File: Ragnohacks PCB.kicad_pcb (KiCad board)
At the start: 2 copper layers, 85.6 x 54 mm, 35 parts, among them J1 Conn_01x02, J2 Conn_01x18, J3 Conn_01x18, J4 USB_A, SW1 SW_Push, U1 RP2040, U2 W25Q128JVS, U3 LD1117S33TR_SOT223, U4 USBLC6-2P6, Y1 12MHz

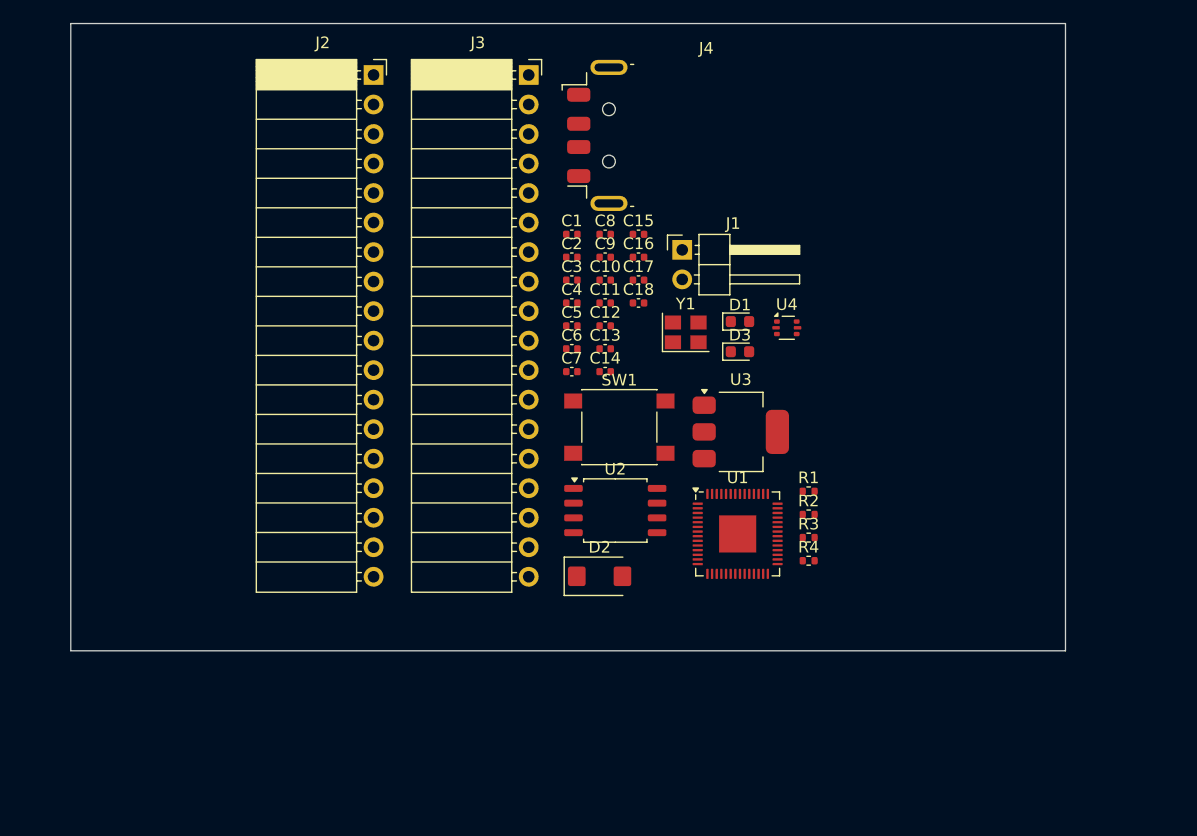
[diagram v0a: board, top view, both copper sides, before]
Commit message: Finish schematic and part choosing, get initial quote
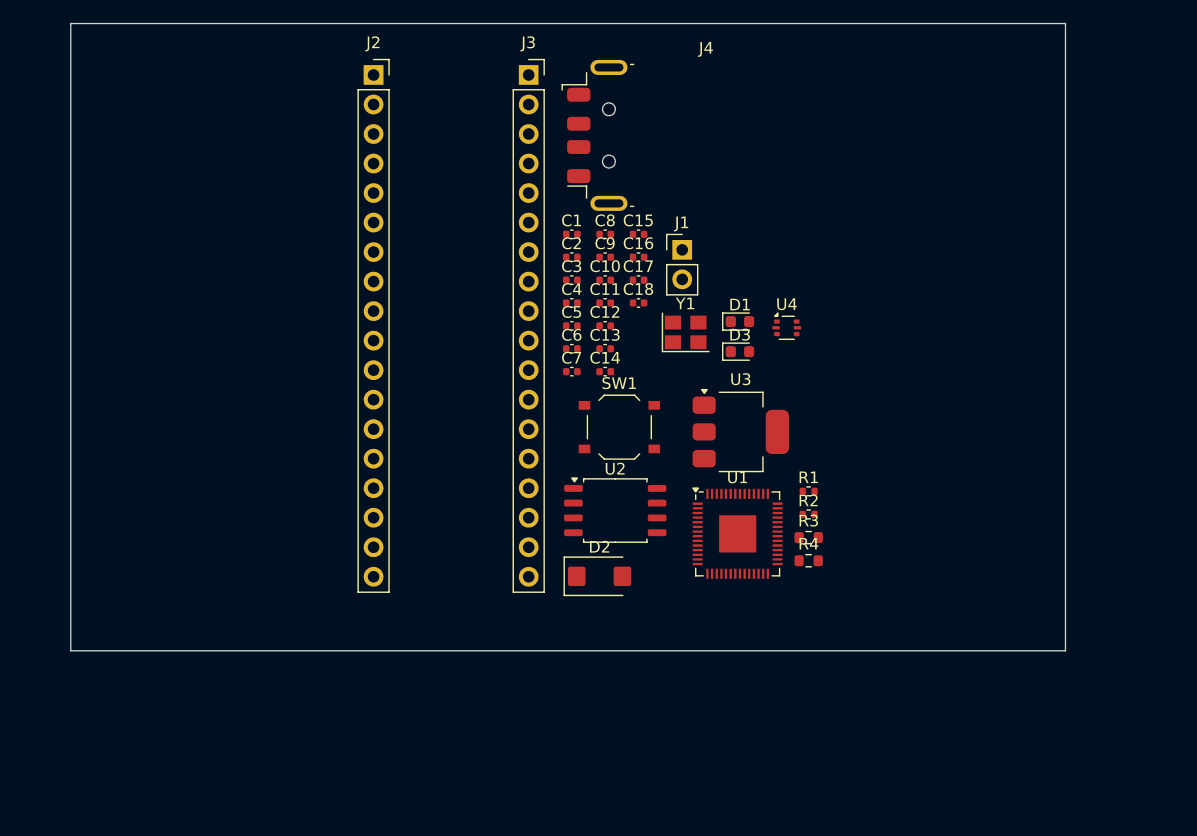
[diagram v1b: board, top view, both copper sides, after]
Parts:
- J1: footprint Connector_PinHeader_2.54mm:PinHeader_1x02_P2.54mm_Horizontal -> Connector_PinHeader_2.54mm:PinHeader_1x02_P2.54mm_Vertical
- J2, J3: footprint Connector_PinSocket_2.54mm:PinSocket_1x18_P2.54mm_Horizontal -> Connector_PinSocket_2.54mm:PinSocket_1x18_P2.54mm_Vertical
- R3, R4: value 460R -> 360R; footprint Resistor_SMD:R_0402_1005Metric -> Resistor_SMD:R_0603_1608Metric
- SW1: footprint Button_Switch_SMD:SW_Push_1P1T_NO_6x6mm_H9.5mm -> Button_Switch_SMD:SW_Push_1P1T_XKB_TS-1187A

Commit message: Start layout, add PCBWay parts
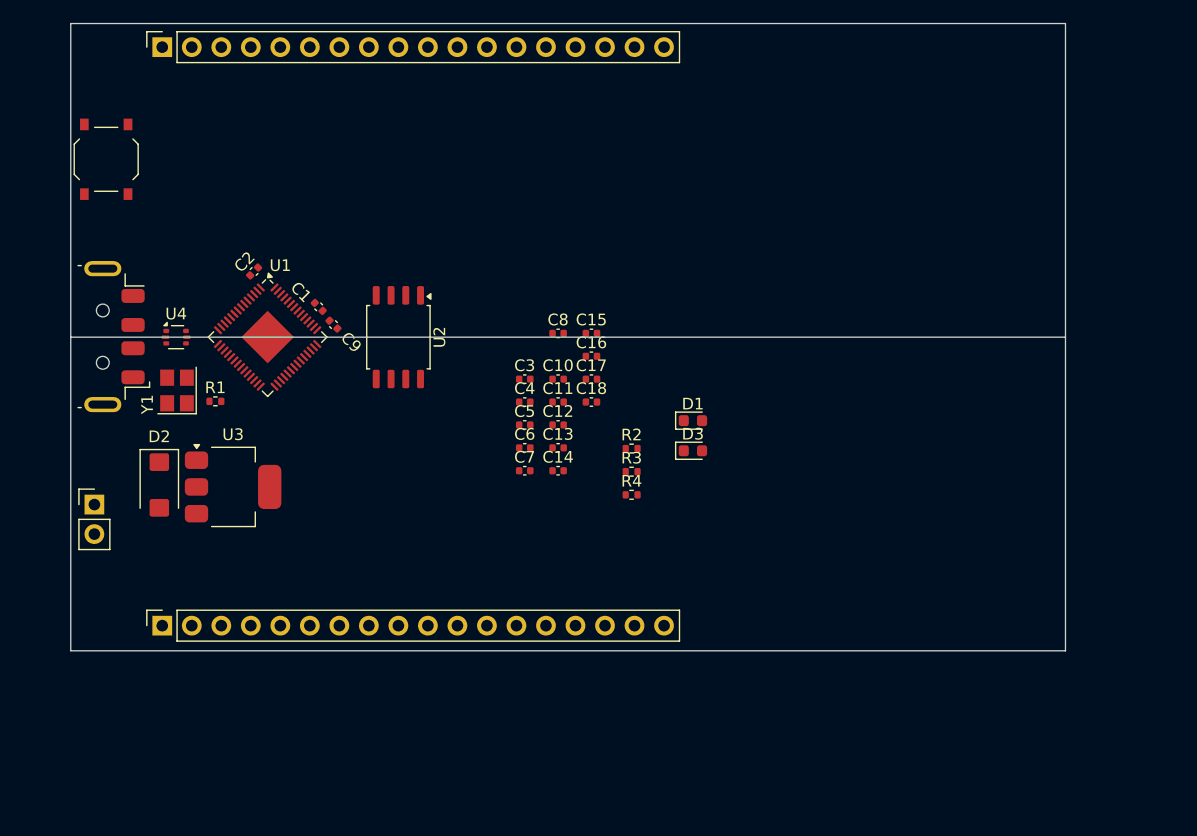
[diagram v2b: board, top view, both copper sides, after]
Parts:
- C13, C14: value 24pF -> 18pF
- R3, R4: footprint Resistor_SMD:R_0603_1608Metric -> Resistor_SMD:R_0402_1005Metric
- moved J4 62.7 mm to (88.6, 91.0), turned to 180 degrees
- moved J1 55.1 mm to (96.3, 105.4)
- moved U4 52.6 mm to (103.3, 91.0)
- moved R1 51.6 mm to (106.7, 96.5)
- moved J2 50.8 mm to (102.1, 115.8), turned to 90 degrees
- moved SW1 49.8 mm to (97.3, 75.7), turned to 90 degrees
- moved Y1 44.1 mm to (103.4, 95.6), turned to 90 degrees
- moved U3 43.9 mm to (108.2, 103.9)
- moved U1 43.8 mm to (111.2, 91.0), turned to -45 degrees
- moved D2 38.7 mm to (101.9, 103.7), turned to -90 degrees
- moved J3 31.6 mm to (102.1, 66.0), turned to 90 degrees
- moved C2 27.4 mm to (110.0, 85.3), turned to 45 degrees
- moved C9 24.1 mm to (116.8, 89.9), turned to -45 degrees
- moved U2 23.9 mm to (122.4, 91.0), turned to -90 degrees
- moved C1 22.7 mm to (115.6, 88.4), turned to -45 degrees
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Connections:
- U1 pad 11: D8 -> D17
- U1 pad 12: D9 -> D16
- U1 pad 13: D10 -> D15
- U1 pad 14: D11 -> D14
- U1 pad 15: D12 -> D13
- U1 pad 16: D13 -> D12
- U1 pad 17: D14 -> D11
- U1 pad 18: D15 -> D10
- U1 pad 2: D0 -> LED_25
- U1 pad 27: D16 -> D9
- U1 pad 28: D17 -> D8
- U1 pad 29: D18 -> D7
- U1 pad 3: D1 -> D24
- U1 pad 30: D19 -> D6
- U1 pad 31: D20 -> D5
- U1 pad 32: D21 -> D4
- U1 pad 34: D22 -> D3
- U1 pad 35: D23 -> D2
- U1 pad 36: D24 -> D1
- U1 pad 37: LED_25 -> D0
- U1 pad 38: A0 -> A3
- U1 pad 39: A1 -> A2
- U1 pad 4: D2 -> D23
- U1 pad 40: A2 -> A1
- U1 pad 41: A3 -> A0
- U1 pad 5: D3 -> D22
- U1 pad 6: D4 -> D21
- U1 pad 7: D5 -> D20
- U1 pad 8: D6 -> D19
- U1 pad 9: D7 -> D18
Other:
- outline, holes or cut-outs redrawn

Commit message: Start tracing
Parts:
- moved C17 44.2 mm to (107.4, 125.4), turned to 180 degrees
- moved R2 34.6 mm to (108.6, 93.9), turned to -90 degrees
- moved C18 33.0 mm to (117.0, 121.1), turned to -90 degrees
- moved C16 32.5 mm to (106.5, 93.4)
- moved C2 26.8 mm to (130.4, 102.7), turned to -45 degrees
- moved C1 24.9 mm to (128.3, 109.8)
- moved C8 23.0 mm to (123.0, 109.6), turned to -135 degrees
- moved J1 22.9 mm to (92.1, 128.0)
- moved C9 22.7 mm to (126.3, 110.6), turned to -135 degrees
- moved U2 19.8 mm to (135.5, 105.9)
- moved C13 19.3 mm to (117.4, 96.1), turned to -90 degrees
- moved C15 19.3 mm to (139.1, 109.9), turned to 90 degrees
- moved C10 19.0 mm to (127.1, 111.3), turned to -135 degrees
- moved U1 18.7 mm to (124.7, 103.9), turned to -135 degrees
- moved C14 18.3 mm to (120.1, 93.7)
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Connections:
- U1 pad 14: D14 -> D0
- U1 pad 15: D13 -> D1
- U1 pad 16: D12 -> D2
- U1 pad 17: D11 -> D3
- U1 pad 18: D10 -> D4
- U1 pad 27: D9 -> D5
- U1 pad 28: D8 -> D6
- U1 pad 30: D6 -> D8
- U1 pad 31: D5 -> D9
- U1 pad 32: D4 -> D10
- U1 pad 34: D3 -> D11
- U1 pad 35: D2 -> D12
- U1 pad 36: D1 -> D13
- U1 pad 37: D0 -> D14
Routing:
- net D0: track 0.00 -> 62.2 mm
- net D1: track 0.00 -> 59.4 mm
- net D2: track 0.00 -> 56.3 mm
- net D15: track 0.00 -> 28.4 mm
- net D16: track 0.00 -> 26.2 mm
- net D18: track 0.00 -> 26.1 mm
- net D19: track 0.00 -> 25.8 mm
- net D17: track 0.00 -> 25.7 mm
- net D24: track 0.00 -> 25.7 mm
- net D20: track 0.00 -> 25.6 mm
- net D21: track 0.00 -> 25.3 mm
- net D22: track 0.00 -> 25.1 mm
- net D23: track 0.00 -> 24.8 mm
- net +3V3: track 0.00 -> 20.5 mm
- net FLASH_CS: track 0.00 -> 12.9 mm
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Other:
- outline, holes or cut-outs redrawn
- board text added: "ON"

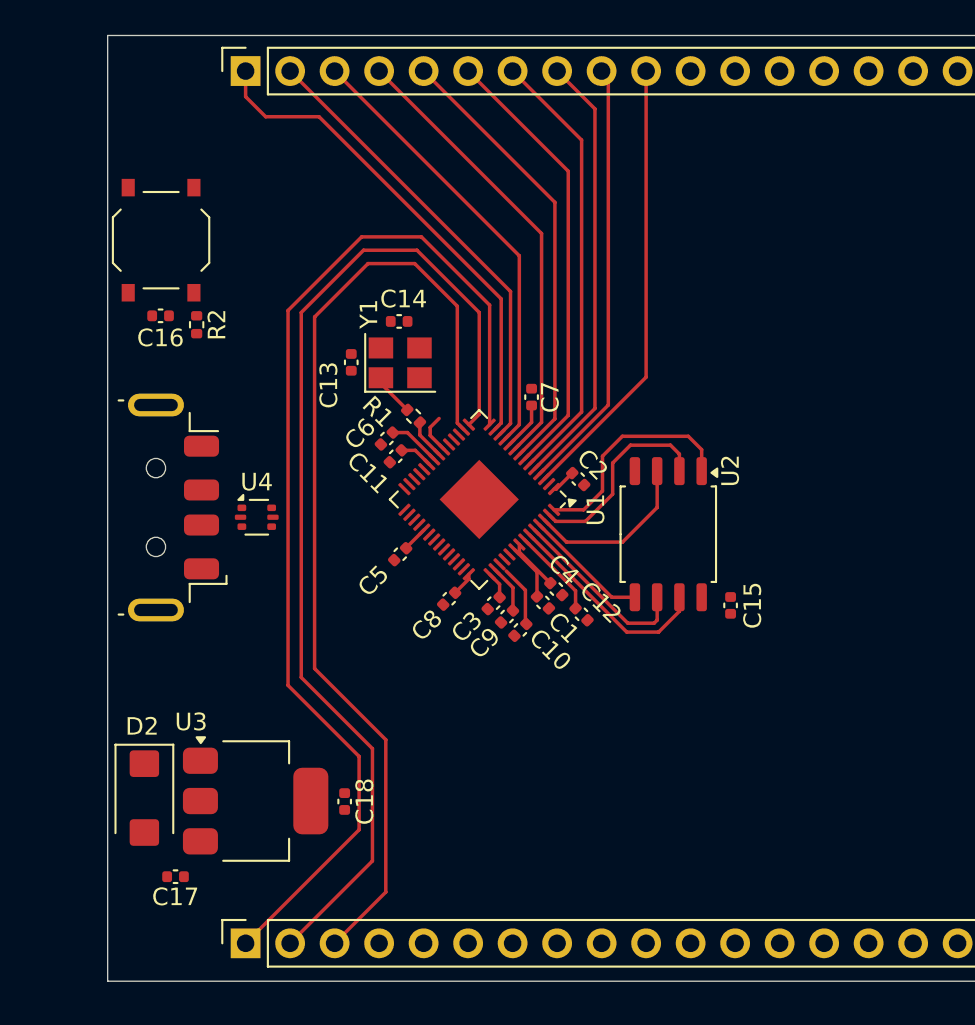
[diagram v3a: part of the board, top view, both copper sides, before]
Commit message: Finish tracing pins
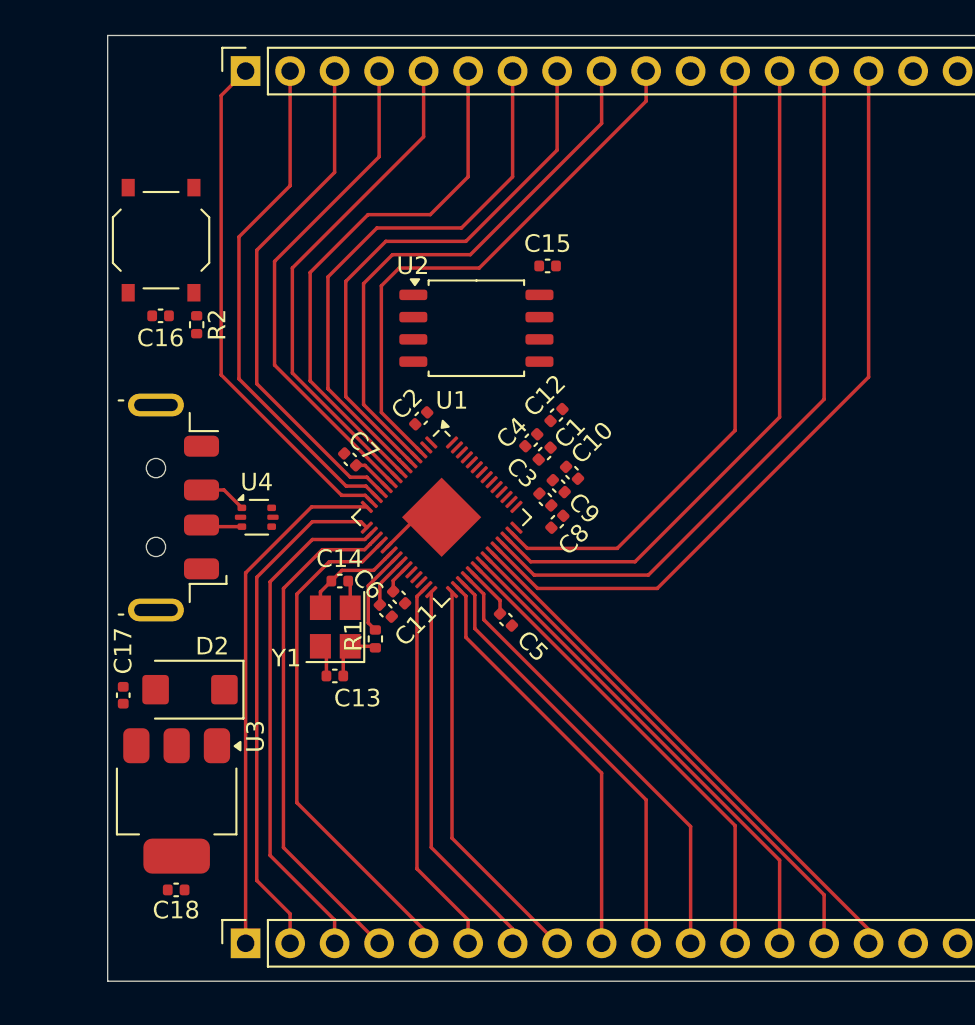
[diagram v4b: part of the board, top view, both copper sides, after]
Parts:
- moved C15 22.0 mm to (128.6, 90.6), turned to 180 degrees
- moved C13 17.9 mm to (116.5, 114.0), turned to 0 degrees
- moved U2 16.1 mm to (124.6, 94.1), turned to 0 degrees
- moved Y1 15.5 mm to (116.5, 111.2), turned to 90 degrees
- moved C14 15.2 mm to (116.8, 108.5), turned to 180 degrees
- moved R1 12.9 mm to (118.8, 111.8), turned to 90 degrees
- moved C12 11.5 mm to (129.1, 99.1), turned to 45 degrees
- moved C7 10.9 mm to (117.3, 101.6), turned to 135 degrees
- moved C18 10.9 mm to (107.4, 126.2), turned to 180 degrees
- moved C17 10.8 mm to (104.4, 115.1), turned to 90 degrees
- moved C6 9.83 mm to (119.4, 110.2), turned to -45 degrees
- moved C2 9.61 mm to (121.4, 99.3), turned to 45 degrees
- moved C10 9.44 mm to (130.0, 102.4), turned to -45 degrees
- moved C4 8.62 mm to (127.7, 100.5), turned to 45 degrees
- moved C1 8.50 mm to (128.4, 101.3), turned to 45 degrees
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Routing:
- net A3: track 0.00 -> 44.7 mm
- net A2: track 0.00 -> 42.1 mm
- net A1: track 0.00 -> 39.3 mm
- net A0: track 0.00 -> 36.4 mm
- net D0: track 62.2 -> 29.6 mm
- net D14: track 0.00 -> 31.2 mm
- net D13: track 0.00 -> 30.0 mm
- net D1: track 59.4 -> 29.4 mm
- net D3: track 0.00 -> 29.0 mm
- net D4: track 0.00 -> 29.0 mm
- net D12: track 0.00 -> 28.8 mm
- net D11: track 0.00 -> 27.6 mm
- net D2: track 56.3 -> 29.1 mm
- net D10: track 0.00 -> 26.2 mm
- net D9: track 0.00 -> 25.0 mm
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
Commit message: Finish tracing
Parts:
- moved J1 38.2 mm to (105.7, 92.2)
- moved R4 33.9 mm to (133.3, 90.7), turned to 90 degrees
- moved R3 30.6 mm to (135.9, 90.7), turned to 90 degrees
- moved D3 30.6 mm to (133.3, 93.2), turned to -90 degrees
- moved D1 26.7 mm to (135.9, 93.2), turned to -90 degrees
- moved C16 4.26 mm to (106.3, 89.2)
- moved R2 4.26 mm to (108.3, 89.7)
- moved SW1 4.25 mm to (106.4, 84.8)
- moved R1 2.07 mm to (118.5, 113.9), turned to 0 degrees
- moved C17 0.55 mm to (104.5, 115.6)
- moved C6 0.52 mm to (119.5, 110.7)
- moved C11 0.51 mm to (120.1, 110.0)
- moved C2 0.25 mm to (121.2, 99.3)
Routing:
- net +3V3: track 8.22 -> 180.3 mm, vias 0 -> 10
- net +5V: track 0.00 -> 122.2 mm, vias 0 -> 1
- net RESET: track 0.00 -> 121.5 mm, vias 0 -> 5
- net +1V1: track 1.69 -> 34.4 mm, vias 0 -> 2
- net USB_DP: track 0.00 -> 23.6 mm, vias 0 -> 2
- net Net-(J1-Pin_2): track 0.00 -> 23.2 mm, vias 0 -> 1
- net Net-(J1-Pin_1): track 0.00 -> 22.8 mm, vias 0 -> 1
- net USB_DN: track 0.00 -> 22.3 mm, vias 0 -> 2
- net LED_25: track 0.00 -> 17.8 mm, vias 0 -> 2
- net FLASH_CS: track 0.00 -> 12.7 mm
- net FLASH_SD3: track 0.00 -> 12.3 mm
- net FLASH_SD1: track 0.00 -> 11.9 mm
- net FLASH_CLK: track 0.00 -> 10.3 mm
- net GND: track 7.26 -> 17.4 mm, vias 0 -> 17
- net FLASH_SD2: track 0.00 -> 8.68 mm
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- added copper zone on B.Cu, net GND
- added copper zone on F.Cu, net GND

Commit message: The finishing touches
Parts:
- J4: footprint Connector_USB:USB_A_Molex_48037-2200_Horizontal -> Connector_USB:USB_A_Keystone_931_Horizontal
- moved J4 20.6 mm to (118.5, 104.3), turned to -90 degrees
- moved C16 2.84 mm to (108.0, 91.4), turned to 90 degrees
- moved R2 1.89 mm to (109.0, 91.4)
- moved SW1 1.78 mm to (106.4, 86.6)
- moved C18 0.28 mm to (107.7, 126.2)
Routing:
- net LED_25: track 17.8 -> 19.6 mm
- net RESET: track 121.5 -> 123.1 mm
- net +3V3: track 180.3 -> 178.9 mm
- net +5V: track 122.2 -> 123.0 mm
- net GND: track 17.4 -> 17.6 mm, vias 17 -> 18
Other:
- outline, holes or cut-outs redrawn
- board text added: "3.3V"
- board text added: "5V"
- board text added: "A0"
- board text added: "A1"
- board text added: "A2"
- board text added: "A3"
- board text added: "D0"
- board text added: "D1"
- board text added: "D10"
- board text added: "D11"
- board text added: "D12"
- board text added: "D14"
- board text added: "D15"
- board text added: "D16"
- board text added: "D17"
- board text added: "D18"
- board text added: "D19"
- board text added: "D2"
- board text added: "D20"
- board text added: "D21"
- board text added: "D22"
- board text added: "D23"
- board text added: "D24"
- board text added: "D3"
- board text added: "D4"
- board text added: "D5"
- board text added: "D6"
- board text added: "D7"
- board text added: "D8"
- board text added: "D9"
- board text added: "GND"
- board text added: "RESET"
- board text added: "VIN"
